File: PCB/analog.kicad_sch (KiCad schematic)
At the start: 13 parts, among them U3 74HC4051, U4 OPA350

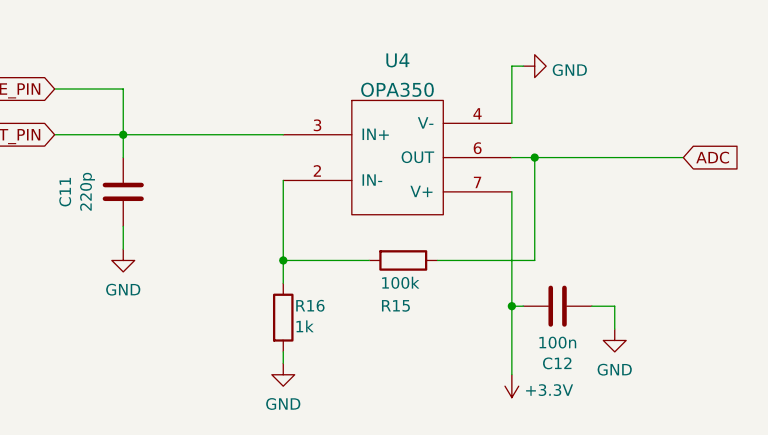
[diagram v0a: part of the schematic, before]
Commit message: Kicad 7 update and change of resistor value
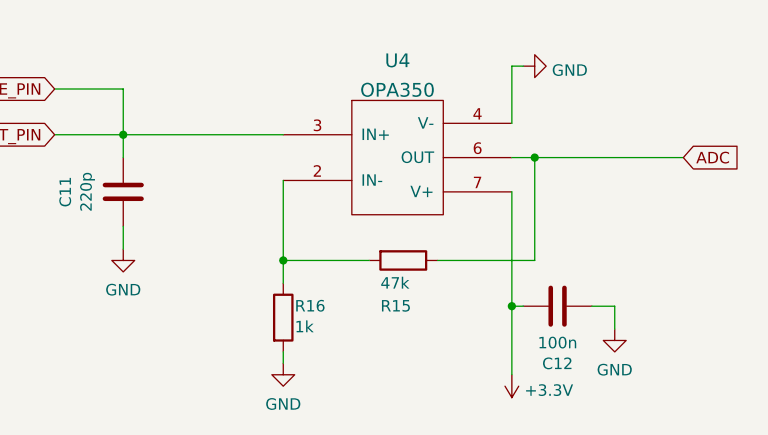
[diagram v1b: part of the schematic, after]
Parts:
- R15: value 100k -> 47k; LCSC C25741 -> C25792

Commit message: Updated to `Rev 1.1`
Updated the title block in schematics to reflect company name and updated EC pads to latest model.
This update isn't critical, hence the lack of proper `Rev` update in README.
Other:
- company: Cipulot PCB Design -> LU.SV Solutions
- title: EC23U - Analog -> EC23U
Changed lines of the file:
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@@
   (paper "A5")
   (title_block
-    (title "EC23U - Analog")
-    (date "2022-11-18")
-    (rev "1")
-    (company "Cipulot PCB Design")
-    (comment 1 "MIT License")
-    (comment 2 "Cipulot")
+    (title "EC23U")
+    (date "2023-07-15")
+    (rev "1.1")
+    (company "LU.SV Solutions")
+    (comment 1 "Cipulot PCB Design")
+    (comment 2 "MIT License")
+    (comment 3 "Cipulot")
   )
   (junction (at 144.145 85.09) (diameter 0) (color 0 0 0 0)
